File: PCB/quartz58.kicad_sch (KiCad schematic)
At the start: 194 parts, among them J1 OLED_128x32, J2 OLED_128x32, J3 Conn_01x10_Socket, J4 Conn_01x10_Pin, SW1 SW_SPDT, SW2 SW_Push, SW3 SW_SPDT, SW4 SW_Push, T1 TPS65-201A-S, U1 Nice_Nano_V2, U2 Nice_Nano_V2

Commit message: updates to pcb
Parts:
- T1: footprint (none) -> Connector_FFC-FPC:Hirose_FH12-6S-0.5SH_1x06-1MP_P0.50mm_Horizontal
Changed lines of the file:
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@@
 			)
 		)
-		(property "Footprint" ""
+		(property "Footprint" "Connector_FFC-FPC:Hirose_FH12-6S-0.5SH_1x06-1MP_P0.50mm_Horizontal"
 			(at 288.29 185.42 0)
 			(effects

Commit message: more progress
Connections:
- net R-COL1: now also U2.12 (9); no longer U2.14 (16)
- net R-COL2: now also U2.11 (8); no longer U2.15 (14)
- net R-COL3: now also U2.10 (7); no longer U2.16 (15)
- net R-COL4: now also U2.9 (6); no longer U2.17 (18)
- net R-COL5: now also U2.8 (5); no longer U2.18 (19)
- net R-ROW0: now also U2.18 (19); no longer U2.8 (5)
- net R-ROW1: now also U2.17 (18); no longer U2.9 (6)
- net R-ROW2: now also U2.16 (15); no longer U2.10 (7)
- net R-ROW3: now also U2.15 (14); no longer U2.11 (8)
- net R-ROW4: now also U2.14 (16); no longer U2.12 (9)
- net +3V8: no longer names the net of SW3.2 (B), U2.24 (B+)

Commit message: updates
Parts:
- BT1, BT2: footprint ScottoKeebs_Components:Connector_1x02_JST-PH -> Connector_JST:JST_PH_S2B-PH-K_1x02_P2.00mm_Horizontal
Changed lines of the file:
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@@
 			)
 		)
-		(property "Footprint" "ScottoKeebs_Components:Connector_1x02_JST-PH"
+		(property "Footprint" "Connector_JST:JST_PH_S2B-PH-K_1x02_P2.00mm_Horizontal"
 			(at 101.346 173.99 90)
 			(effects
@@
 			)
 		)
-		(property "Footprint" "ScottoKeebs_Components:Connector_1x02_JST-PH"
+		(property "Footprint" "Connector_JST:JST_PH_S2B-PH-K_1x02_P2.00mm_Horizontal"
 			(at 388.366 177.8 90)
 			(effects

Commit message: BOM and Schem updates
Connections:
- net +3V3: no longer D100.3 (VSS), D101.3 (VSS), D102.3 (VSS), D103.3 (VSS), D104.3 (VSS), D105.3 (VSS), D106.3 (VSS), D107.3 (VSS), D108.3 (VSS), D109.3 (VSS), D110.3 (VSS), D111.3 (VSS), D112.3 (VSS), D113.3 (VSS), D114.3 (VSS), D115.3 (VSS), D116.3 (VSS), D117.3 (VSS), D118.3 (VSS), D119.3 (VSS), D120.3 (VSS), D34.3 (VSS), D35.3 (VSS), D36.3 (VSS), D37.3 (VSS), D38.3 (VSS), D39.3 (VSS), D40.3 (VSS), D41.3 (VSS), D42.3 (VSS), D43.3 (VSS), D44.3 (VSS), D45.3 (VSS), D46.3 (VSS), D47.3 (VSS), D48.3 (VSS), D49.3 (VSS), D50.3 (VSS), D51.3 (VSS), D52.3 (VSS), D53.3 (VSS), D54.3 (VSS), D55.3 (VSS), D56.3 (VSS), D57.3 (VSS), D58.3 (VSS), D59.3 (VSS), D60.3 (VSS), D61.3 (VSS), D62.3 (VSS), D92.3 (VSS), D93.3 (VSS), D94.3 (VSS), D95.3 (VSS), D96.3 (VSS), D97.3 (VSS), D98.3 (VSS), D99.3 (VSS)
- net GND: no longer D100.1 (VDD), D101.1 (VDD), D102.1 (VDD), D103.1 (VDD), D104.1 (VDD), D105.1 (VDD), D106.1 (VDD), D107.1 (VDD), D108.1 (VDD), D109.1 (VDD), D110.1 (VDD), D111.1 (VDD), D112.1 (VDD), D113.1 (VDD), D114.1 (VDD), D115.1 (VDD), D116.1 (VDD), D117.1 (VDD), D118.1 (VDD), D119.1 (VDD), D120.1 (VDD), D34.1 (VDD), D35.1 (VDD), D36.1 (VDD), D37.1 (VDD), D38.1 (VDD), D39.1 (VDD), D40.1 (VDD), D41.1 (VDD), D42.1 (VDD), D43.1 (VDD), D44.1 (VDD), D45.1 (VDD), D46.1 (VDD), D47.1 (VDD), D48.1 (VDD), D49.1 (VDD), D50.1 (VDD), D51.1 (VDD), D52.1 (VDD), D53.1 (VDD), D54.1 (VDD), D55.1 (VDD), D56.1 (VDD), D57.1 (VDD), D58.1 (VDD), D59.1 (VDD), D60.1 (VDD), D61.1 (VDD), D62.1 (VDD), D92.1 (VDD), D93.1 (VDD), D94.1 (VDD), D95.1 (VDD), D96.1 (VDD), D97.1 (VDD), D98.1 (VDD), D99.1 (VDD), U1.4 (GND), U2.4 (GND)
- net L-RAW: now reaches SW1.2 (B), U1.24 (B+)
- net L-RAW: now also D34.3 (VSS), D35.3 (VSS), D36.3 (VSS), D37.3 (VSS), D38.3 (VSS), D39.3 (VSS), D40.3 (VSS), D41.3 (VSS), D42.3 (VSS), D43.3 (VSS), D44.3 (VSS), D45.3 (VSS), D46.3 (VSS), D47.3 (VSS), D48.3 (VSS), D49.3 (VSS), D50.3 (VSS), D51.3 (VSS), D52.3 (VSS), D53.3 (VSS), D54.3 (VSS), D55.3 (VSS), D56.3 (VSS), D57.3 (VSS), D58.3 (VSS), D59.3 (VSS), D60.3 (VSS), D61.3 (VSS), D62.3 (VSS)
- net R-RAW: now reaches SW3.2 (B), U2.24 (B+)
- net R-RAW: now also D100.3 (VSS), D101.3 (VSS), D102.3 (VSS), D103.3 (VSS), D104.3 (VSS), D105.3 (VSS), D106.3 (VSS), D107.3 (VSS), D108.3 (VSS), D109.3 (VSS), D110.3 (VSS), D111.3 (VSS), D112.3 (VSS), D113.3 (VSS), D114.3 (VSS), D115.3 (VSS), D116.3 (VSS), D117.3 (VSS), D118.3 (VSS), D119.3 (VSS), D120.3 (VSS), D92.3 (VSS), D93.3 (VSS), D94.3 (VSS), D95.3 (VSS), D96.3 (VSS), D97.3 (VSS), D98.3 (VSS), D99.3 (VSS)
- new net L-RGBGND: D34.1 (VDD), D35.1 (VDD), D36.1 (VDD), D37.1 (VDD), D38.1 (VDD), D39.1 (VDD), D40.1 (VDD), D41.1 (VDD), D42.1 (VDD), D43.1 (VDD), D44.1 (VDD), D45.1 (VDD), D46.1 (VDD), D47.1 (VDD), D48.1 (VDD), D49.1 (VDD), D50.1 (VDD), D51.1 (VDD), D52.1 (VDD), D53.1 (VDD), D54.1 (VDD), D55.1 (VDD), D56.1 (VDD), D57.1 (VDD), D58.1 (VDD), D59.1 (VDD), D60.1 (VDD), D61.1 (VDD), D62.1 (VDD), U1.4 (GND)
- new net R-RGBGND: D100.1 (VDD), D101.1 (VDD), D102.1 (VDD), D103.1 (VDD), D104.1 (VDD), D105.1 (VDD), D106.1 (VDD), D107.1 (VDD), D108.1 (VDD), D109.1 (VDD), D110.1 (VDD), D111.1 (VDD), D112.1 (VDD), D113.1 (VDD), D114.1 (VDD), D115.1 (VDD), D116.1 (VDD), D117.1 (VDD), D118.1 (VDD), D119.1 (VDD), D120.1 (VDD), D92.1 (VDD), D93.1 (VDD), D94.1 (VDD), D95.1 (VDD), D96.1 (VDD), D97.1 (VDD), D98.1 (VDD), D99.1 (VDD), U2.4 (GND)

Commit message: updates to pcb and BOM
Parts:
- removed D100, D101, D102, D103, D104, D105, D106, D107, D108, D109, D110, D111, D112, D113, D114, D115, D116, D117, D118, D119, D120, D34, D35, D36, D37, D38, D39, D40, D41, D42, D43, D44, D45, D46, D47, D48, D49, D50, D51, D52, D53, D54, D55, D56, D57, D58, D59, D60, D61, D62, D92, D93, D94, D95, D96, D97, D98, D99: LED_SK6812MINI, Keebio-Parts.pretty-master:SK6812-MINI-E, symbol ScottoKeebs:LED_SK6812MINI
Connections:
- net L-RGB is gone; now on net L-CS: U1.1
- net L-RGBGND is gone; now on net GND: U1.4 (GND)
- net R-RGBGND is gone; now on net GND: U2.4 (GND)
- net L-CS: no longer U1.2 (0)
- net SW1: now also U1.2 (0); no longer U1.25 (1)
- net L-RAW: no longer names the net of SW1.2 (B), U1.24 (B+)
- net R-RAW: no longer names the net of SW3.2 (B), U2.24 (B+)
- net R-RGB: no longer names the net of U2.1
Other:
- note removed: "RGB"
- moved on the sheet: BT1, BT2, D1, D10, D11, D12, D13, D14, D15, D16, D17, D18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

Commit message: borderline, caught between the tides of pain and rapture
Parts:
- removed BT1, BT2: Battery_Cell, Connector_JST:JST_PH_S2B-PH-K_1x02_P2.00mm_Horizontal, symbol Device:Battery_Cell
- added J5, J6: JST_02, Connector_JST:JST_PH_S2B-PH-K_1x02_P2.00mm_Horizontal, symbol PCM_SL_Connectors:JST_02
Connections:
- net GND: now also J5.1, J6.1
- net L-BATTERY-POSITIVE: now also J5.2
- net L-COL0: now also U1.18 (19); no longer U1.17 (18)
- net L-COL1: now also U1.17 (18); no longer U1.16 (15)
- net L-COL2: now also U1.16 (15); no longer U1.15 (14)
- net L-COL3: now also U1.15 (14); no longer U1.14 (16)
- net L-COL4: now also U1.14 (16); no longer U1.13 (10)
- net L-COL5: now also U1.13 (10); no longer U1.18 (19)
- net R-BATTERY-POSITIVE: now also J6.2

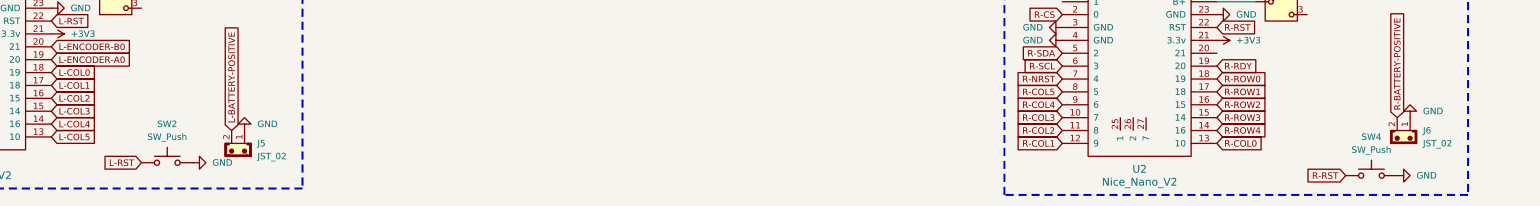
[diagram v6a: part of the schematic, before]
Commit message: bom optimizations
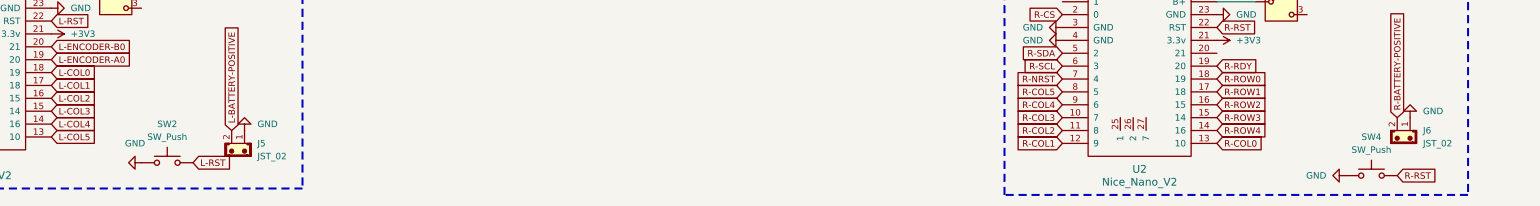
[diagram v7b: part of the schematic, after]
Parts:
- SW2, SW4: footprint ul_EVQ-PUJ02K:SW_EVQPUJ_4P7X3P5_PAN -> Button_Switch_SMD:Panasonic_EVQPUL_EVQPUC
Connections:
- net GND: now also SW2.1, SW4.1; no longer SW2.2, SW4.2
- net L-RST: now also SW2.2; no longer SW2.1
- net R-RST: now also SW4.2; no longer SW4.1
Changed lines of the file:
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@@
 		)
 	)
+	(global_label "R-RST"
+		(shape input)
+		(at 326.39 210.82 0)
+		(fields_autoplaced yes)
+		(effects
+			(font
+				(size 1.27 1.27)
+			)
+			(justify left)
+		)
+		(property "Intersheetrefs" "${INTERSHEET_REFS}"
+			(at 335.6647 210.82 0)
+			(effects
+				(font
+					(size 1.27 1.27)
+				)
+				(justify left)
+				(hide yes)
+			)
+		)
+	)
 	(global_label "R-COL1"
 		(shape input)
@@
 		)
 	)
-	(global_label "R-RST"
-		(shape input)
-		(at 316.23 210.82 180)
-		(fields_autoplaced yes)
-		(effects
-			(font
-				(size 1.27 1.27)
-			)
-			(justify right)
-		)
-		(property "Intersheetrefs" "${INTERSHEET_REFS}"
-			(at 306.9553 210.82 0)
-			(effects
-				(font
-					(size 1.27 1.27)
-				)
-				(justify right)
-				(hide yes)
-			)
-		)
-	)
 	(global_label "R-SDA"
 		(shape input)
@@
 		)
 	)
-	(global_label "L-RST"
-		(shape input)
-		(at 78.74 208.28 180)
-		(fields_autoplaced yes)
-		(effects
-			(font
-				(size 1.27 1.27)
-			)
-			(justify right)
-		)
-		(property "Intersheetrefs" "${INTERSHEET_REFS}"
-			(at 69.7072 208.28 0)
-			(effects
-				(font
-					(size 1.27 1.27)
-				)
-				(justify right)
-				(hide yes)
-			)
-		)
-	)
 	(global_label "SW5"
 		(shape input)
@@
 		)
 	)
+	(global_label "L-RST"
+		(shape input)
+		(at 88.9 208.28 0)
+		(fields_autoplaced yes)
+		(effects
+			(font
+				(size 1.27 1.27)
+			)
+			(justify left)
+		)
+		(property "Intersheetrefs" "${INTERSHEET_REFS}"
+			(at 97.9328 208.28 0)
+			(effects
+				(font
+					(size 1.27 1.27)
+				)
+				(justify left)
+				(hide yes)
+			)
+		)
+	)
 	(global_label "L-CS"
 		(shape input)
@@
 	(symbol
 		(lib_id "power:GND")
-		(at 88.9 208.28 90)
+		(at 78.74 208.28 270)
 		(unit 1)
 		(exclude_from_sim no)
@@
 		(fields_autoplaced yes)
 		(property "Reference" "#PWR07"
-			(at 95.25 208.28 0)
+			(at 72.39 208.28 0)
 			(effects
 				(font
@@
 		)
 		(property "Value" "GND"
-			(at 92.71 208.2799 90)
+			(at 77.47 204.47 90)
 			(effects
 				(font
 					(size 1.27 1.27)
 				)
-				(justify right)
 			)
 		)
 		(property "Footprint" ""
-			(at 88.9 208.28 0)
+			(at 78.74 208.28 0)
 			(effects
 				(font
@@
 		)
 		(property "Datasheet" ""
-			(at 88.9 208.28 0)
+			(at 78.74 208.28 0)
 			(effects
 				(font
@@
 		)
 		(property "Description" "Power symbol creates a global label with name \"GND\" , ground"
-			(at 88.9 208.28 0)
+			(at 78.74 208.28 0)
 			(effects
 				(font
@@
 	)
 	(symbol
+		(lib_id "power:GND")
+		(at 316.23 210.82 270)
+		(unit 1)
+		(exclude_from_sim no)
+		(in_bom yes)
+		(on_board yes)
+		(dnp no)
+		(fields_autoplaced yes)
+		(property "Reference" "#PWR010"
+			(at 309.88 210.82 0)
+			(effects
+				(font
+					(size 1.27 1.27)
+				)
+				(hide yes)
+			)
+		)
+		(property "Value" "GND"
+			(at 312.42 210.8199 90)
+			(effects
+				(font
+					(size 1.27 1.27)
+				)
+				(justify right)
+			)
+		)
+		(property "Footprint" ""
+			(at 316.23 210.82 0)
+			(effects
+				(font
+					(size 1.27 1.27)
+				)
+				(hide yes)
+			)
+		)
+		(property "Datasheet" ""
+			(at 316.23 210.82 0)
+			(effects
+				(font
+					(size 1.27 1.27)
+				)
+				(hide yes)
+			)
+		)
+		(property "Description" "Power symbol creates a global label with name \"GND\" , ground"
+			(at 316.23 210.82 0)
+			(effects
+				(font
+					(size 1.27 1.27)
+				)
+				(hide yes)
+			)
+		)
+		(pin "1"
+		)
+		(instances
+			(project "quartz58"
+				(path "/a630da1b-27bd-4d59-a0f0-6159ff5296b0"
+					(reference "#PWR010")
+					(unit 1)
+				)
+			)
+		)
+	)
+	(symbol
 		(lib_id "ScottoKeebs:Placeholder_Keyswitch")
 		(at 24.13 119.38 0)
@@
 	)
 	(symbol
-		(lib_id "power:GND")
-		(at 326.39 210.82 90)
-		(unit 1)
-		(exclude_from_sim no)
-		(in_bom yes)
-		(on_board yes)
-		(dnp no)
-		(fields_autoplaced yes)
-		(property "Reference" "#PWR024"
-			(at 332.74 210.82 0)
-			(effects
-				(font
-					(size 1.27 1.27)
-				)
-				(hide yes)
-			)
-		)
-		(property "Value" "GND"
-			(at 330.2 210.8199 90)
-			(effects
-				(font
-					(size 1.27 1.27)
-				)
-				(justify right)
-			)
-		)
-		(property "Footprint" ""
-			(at 326.39 210.82 0)
-			(effects
-				(font
-					(size 1.27 1.27)
-				)
-				(hide yes)
-			)
-		)
-		(property "Datasheet" ""
-			(at 326.39 210.82 0)
-			(effects
-				(font
-					(size 1.27 1.27)
-				)
-				(hide yes)
-			)
-		)
-		(property "Description" "Power symbol creates a global label with name \"GND\" , ground"
-			(at 326.39 210.82 0)
-			(effects
-				(font
-					(size 1.27 1.27)
-				)
-				(hide yes)
-			)
-		)
-		(pin "1"
-		)
-		(instances
-			(project "quartz58"
-				(path "/a630da1b-27bd-4d59-a0f0-6159ff5296b0"
-					(reference "#PWR024")
-					(unit 1)
-				)
-			)
-		)
-	)
-	(symbol
 		(lib_id "ScottoKeebs:OLED_128x32")
 		(at 129.54 58.42 90)
@@
 			)
 		)
-		(property "Footprint" "ul_EVQ-PUJ02K:SW_EVQPUJ_4P7X3P5_PAN"
+		(property "Footprint" "Button_Switch_SMD:Panasonic_EVQPUL_EVQPUC"
 			(at 321.31 205.74 0)
 			(effects
@@
 			)
 		)
-		(property "Footprint" "ul_EVQ-PUJ02K:SW_EVQPUJ_4P7X3P5_PAN"
+		(property "Footprint" "Button_Switch_SMD:Panasonic_EVQPUL_EVQPUC"
 			(at 83.82 203.2 0)
 			(effects
